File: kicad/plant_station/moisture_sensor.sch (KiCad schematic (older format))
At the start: 29 parts, among them IC3 TLC555CDR, IC4 ADC081C021CIMK_NOPB, IC5 IQS263B-0-DNR, IC6 CAP1293-1-AC3-TR

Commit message: Board v.2 sent for printing
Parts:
- removed J?: Conn_02x08_Counter_Clockwise, symbol Connector_Generic:Conn_02x08_Counter_Clockwise
- added J3: Conn_02x08_Odd_Even, Connector_PinHeader_2.54mm:PinHeader_2x08_P2.54mm_Vertical, symbol Connector_Generic:Conn_02x08_Odd_Even
- added J7: Samtec CES-104-01-T-D, Connector_PinSocket_2.54mm:PinSocket_2x04_P2.54mm_Vertical, symbol Connector_Generic:Conn_02x04_Odd_Even
- C4: value 1uF -> 1μF; footprint (none) -> Capacitor_SMD:C_1206_3216Metric
- C5, Cref1: footprint (none) -> Capacitor_SMD:C_1206_3216Metric
- C6: renamed from C?; value 1uF -> 1μF; footprint (none) -> Capacitor_SMD:C_1206_3216Metric
- C7: renamed from C?; value 0.1uF -> 0.1μF; footprint (none) -> Capacitor_SMD:C_1206_3216Metric
- Cdec1: value 0.1uF -> 0.1μF; footprint (none) -> Capacitor_SMD:C_1206_3216Metric
- Cdec2: renamed from Cdec?; value 4.7uF -> 4.7μF; footprint (none) -> Capacitor_SMD:C_1206_3216Metric
- IC6: footprint SON50P300X200X80-9N -> LocalsLib:CAP1293-1-AC3-TR
- J1: renamed from J?; value Conn_01x05 -> Conn_01x05_555; footprint (none) -> Connector_PinHeader_2.54mm:PinHeader_1x05_P2.54mm_Vertical
- J2: renamed from J?; value IQS263 -> Conn_01x04_IQS263; footprint (none) -> Connector_PinHeader_2.54mm:PinHeader_1x04_P2.54mm_Vertical
- J4: renamed from J?; value Conn_01x02 -> Conn_01x02_Sensor; footprint (none) -> Connector_PinHeader_2.54mm:PinHeader_1x02_P2.54mm_Vertical
- J5: renamed from J?; value CAP1293 -> Conn_01x03_CAP1293; footprint (none) -> Connector_PinHeader_2.54mm:PinHeader_1x03_P2.54mm_Vertical
- R10, R11, R5, R7, R8, R9: renamed from R?; footprint (none) -> Resistor_SMD:R_0805_2012Metric
- R12, R13: renamed from R?; value 10K? -> 4K7; footprint (none) -> Resistor_SMD:R_0805_2012Metric
- R4, Rb1: footprint (none) -> Resistor_SMD:R_1206_3216Metric
- R6: renamed from R?; value 5K? -> 4K7; footprint (none) -> Resistor_SMD:R_0805_2012Metric
- Ra1: footprint (none) -> Resistor_SMD:R_0805_2012Metric
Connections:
- net labels added: +3.3V, Sensor_Inside, Sensor_Outside
- wire segments 121 -> 118
- no-connect marks 0 -> 2
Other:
- note added: "Capacitor Inside\nPlate"
- note added: "Capacitor Outside\nPlate"
- note added: "Moisture Sensor"
- note removed: "Capacitor In Pin"
- note removed: "Capacitor Out Pin"
- moved on the sheet: C4, C5, C6, C7, Cdec1, Cdec2, Cref1, D1, IC3, IC4, J2, J4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

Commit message: Started working on v3 - added ADC081 driver and removed CAP and IQS chips
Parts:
- removed C6: 1μF, Capacitor_SMD:C_1206_3216Metric, symbol Device:C
- removed C7: 0.1μF, Capacitor_SMD:C_1206_3216Metric, symbol Device:C
- removed IC5: IQS263B-0-DNR, SamacSys:SON50P300X300X80-11N-D, symbol SamaSys:IQS263B-0-DNR
- removed IC6: CAP1293-1-AC3-TR, LocalsLib:CAP1293-1-AC3-TR, symbol LocalsLib:CAP1293-1-AC3-TR
- removed J2: Conn_01x04_IQS263, Connector_PinHeader_2.54mm:PinHeader_1x04_P2.54mm_Vertical, symbol Connector_Generic:Conn_01x04
- removed J3: Conn_02x08_Odd_Even, Connector_PinHeader_2.54mm:PinHeader_2x08_P2.54mm_Vertical, symbol Connector_Generic:Conn_02x08_Odd_Even
- removed J5: Conn_01x03_CAP1293, Connector_PinHeader_2.54mm:PinHeader_1x03_P2.54mm_Vertical, symbol Connector_Generic:Conn_01x03
- removed R10, R7, R8, R9: 470, Resistor_SMD:R_0805_2012Metric, symbol Device:R
- removed R11: 42.2, Resistor_SMD:R_0805_2012Metric, symbol Device:R
- removed R12, R13: 4K7, Resistor_SMD:R_0805_2012Metric, symbol Device:R
- Cdec2: footprint Capacitor_SMD:C_1206_3216Metric -> (none)
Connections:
- wire segments 118 -> 58
- no-connect marks 2 -> 0
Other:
- note added: "I2C ADDR 0x54"

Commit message: v3 schematics complete, USB breakout PCB designed
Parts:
- removed Cdec2: 4.7μF, symbol Device:C
- removed J1: Conn_01x05_555, Connector_PinHeader_2.54mm:PinHeader_1x05_P2.54mm_Vertical, symbol Connector_Generic:Conn_01x05
- removed J4: Conn_01x02_Sensor, Connector_PinHeader_2.54mm:PinHeader_1x02_P2.54mm_Vertical, symbol Connector_Generic:Conn_01x02
- removed J7: Samtec CES-104-01-T-D, Connector_PinSocket_2.54mm:PinSocket_2x04_P2.54mm_Vertical, symbol Connector_Generic:Conn_02x04_Odd_Even
- removed R6: 4K7, Resistor_SMD:R_0805_2012Metric, symbol Device:R
- added C7: 4.7uF, Capacitor_SMD:C_1206_3216Metric, symbol Device:C
- added D10: LS4148, Parts:MELF_SOD_80_3_BZT55B13GS08, symbol Device:D_Small
- added FB1, FB2: BLM21AG601SZ1D, Parts:Ferrite_Bead_0805_BLM21, symbol Device:Ferrite_Bead
- added J11: SOIL_I2C, Parts:Molex_Conn_SMD_01x06_505567_0671, symbol Parts:505567-0671
- added Q1: DTC113Z, Parts:DTC113ZEBTL, symbol Transistor_BJT:DTC113Z
- D1: footprint Diode_SMD:D_MELF -> Parts:MELF_SOD_80_3_BZT55B13GS08
- renumbered Cdec1 to C3
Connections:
- net labels added: ALL_EN, GNDA, HOST_WAKE, VA, VDD
- net labels removed: +3.3V, +3V3, 555_ALERT, CAP_ALERT, IQS_RDY
- wire segments 58 -> 40
- no-connect marks 0 -> 2
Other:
- note removed: "Capacitor Inside\nPlate"
- note removed: "Capacitor Outside\nPlate"
- moved on the sheet: C3, C4, C5, Cref1, D1, IC3, IC4, R4, R5, Ra1, Rb1

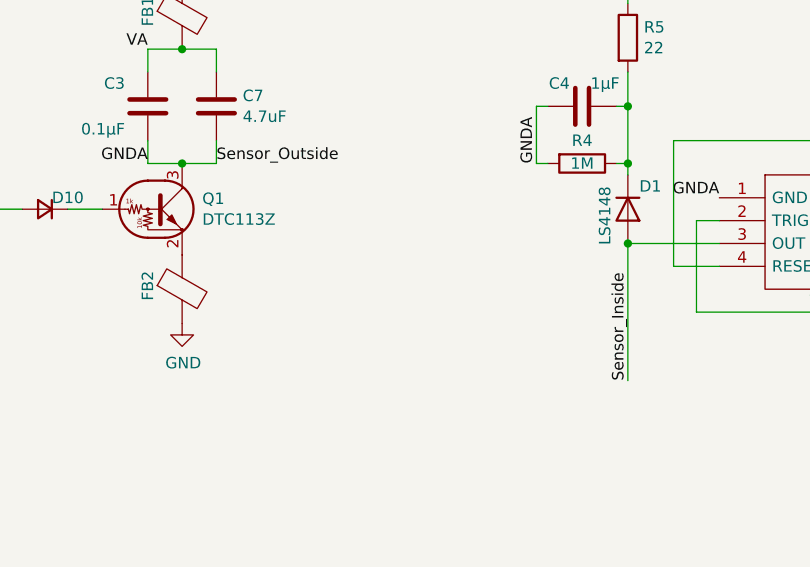
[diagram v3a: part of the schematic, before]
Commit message: Moved the LED driver to LEDs board, refactored connectors. Hopefuly PCBNEW could update it all in place
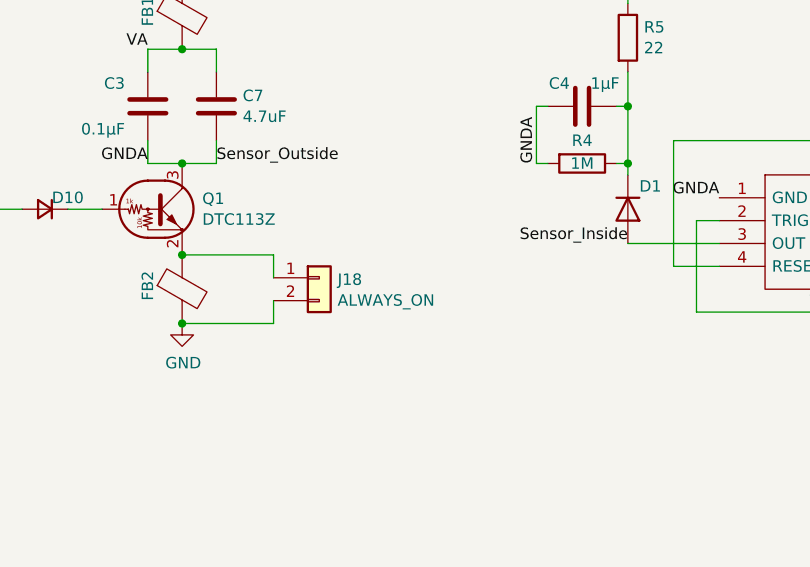
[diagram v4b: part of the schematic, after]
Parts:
- added J18: ALWAYS_ON, Connector_PinHeader_2.54mm:PinHeader_1x02_P2.54mm_Vertical, symbol Connector_Generic:Conn_01x02
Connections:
- net GND: now also J18.2 (Pin_2)
- net at FB2.1, Q1.2 (E): now also J18.1 (Pin_1)
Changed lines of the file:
@@
 P 7150 3900
 F 0 "D1" V 7050 3950 50  0000 L CNN
-F 1 "LS4148" H 7050 3800 50  0000 L CNN
+F 1 "LS4148" H 7050 3800 50  0001 L CNN
 F 2 "Parts:MELF_SOD_80_3_BZT55B13GS08" H 7150 3900 50  0001 C CNN
 F 3 "~" H 7150 3900 50  0001 C CNN
@@
 Wire Wire Line
 	5050 3200 5050 3300
-Text Label 7150 4650 1    50   ~ 0
+Text Label 7150 4050 2    50   ~ 0
 Sensor_Inside
 Text Label 5350 3700 0    50   ~ 0
@@
 Text Label 4400 3900 2    50   ~ 0
 ALL_EN
-Wire Wire Line
-	7150 4050 7150 4650
-Connection ~ 7150 4050
 Text Label 6750 3700 1    50   ~ 0
 GNDA
@@
 	1    0    0    -1
 $EndComp
+$Comp
+L Connector_Generic:Conn_01x02 J18
+U 1 1 5F4FBEBB
+P 5800 4200
+F 0 "J18" H 5880 4192 50  0000 L CNN
+F 1 "ALWAYS_ON" H 5880 4101 50  0000 L CNN
+F 2 "Connector_PinHeader_2.54mm:PinHeader_1x02_P2.54mm_Vertical" H 5800 4200 50  0001 C CNN
+F 3 "~" H 5800 4200 50  0001 C CNN
+	1    5800 4200
+	1    0    0    -1
+$EndComp
+Wire Wire Line
+	5200 4100 5600 4100
+Wire Wire Line
+	5600 4100 5600 4200
+Connection ~ 5200 4100
+Wire Wire Line
+	5600 4300 5600 4400
+Wire Wire Line
+	5600 4400 5200 4400
+Connection ~ 5200 4400
 $EndSCHEMATC

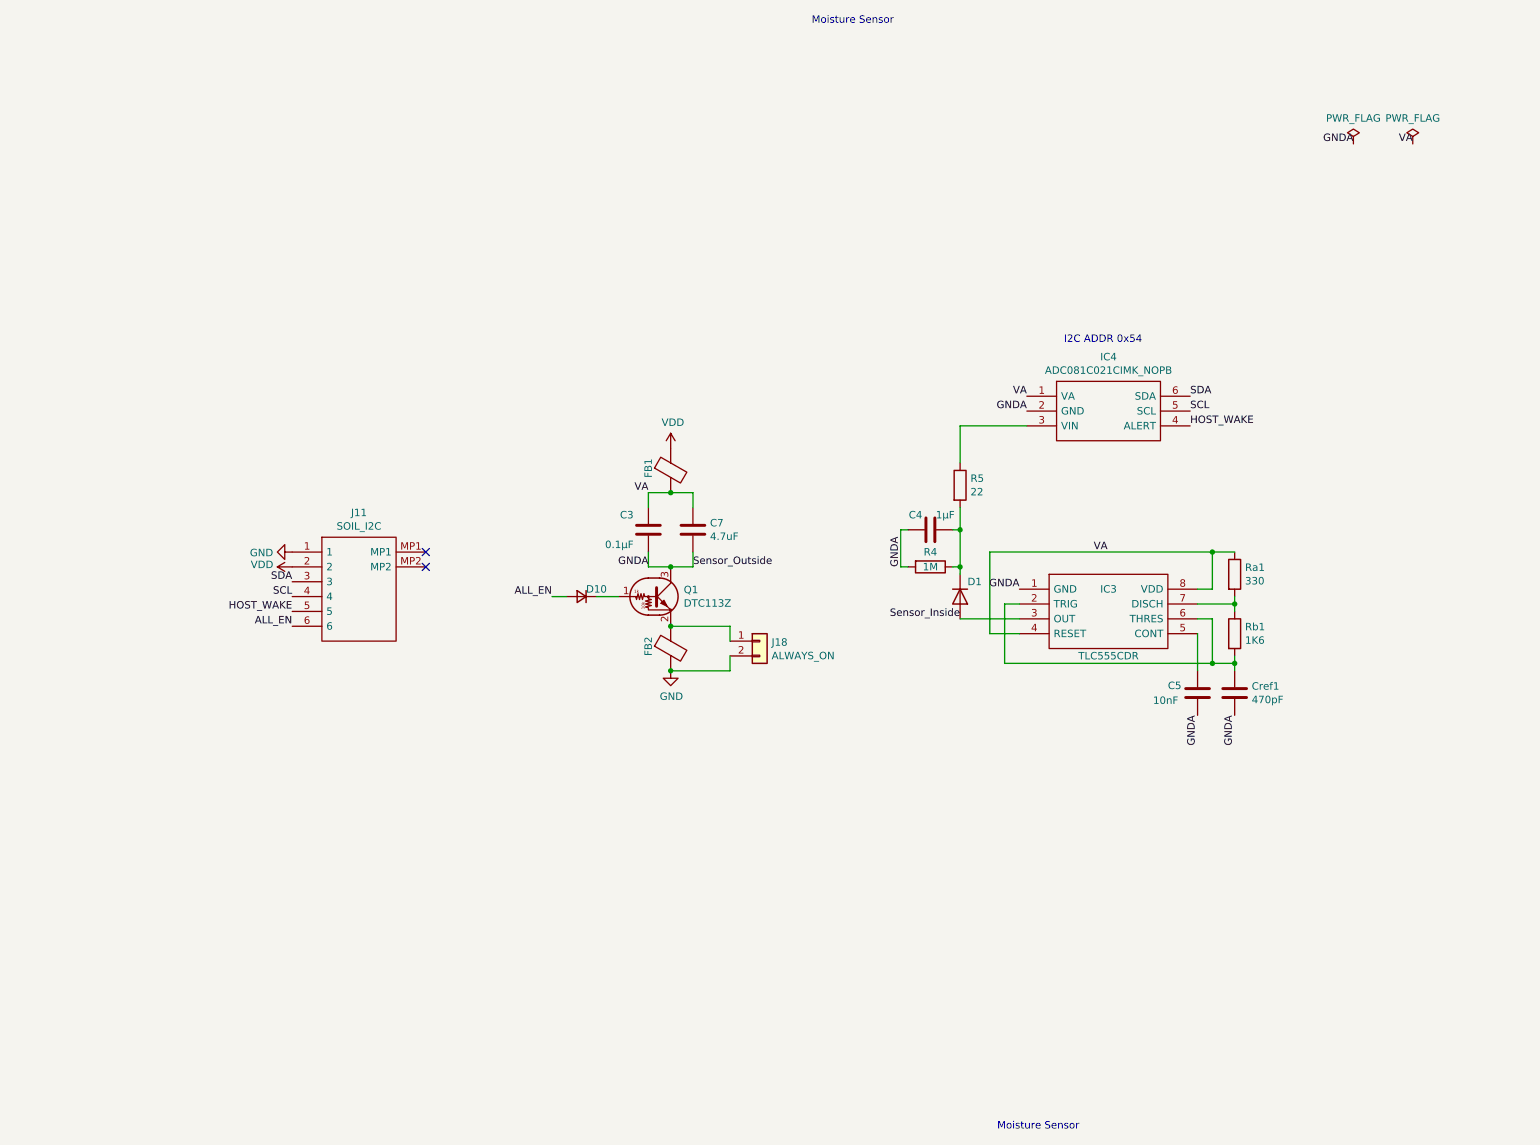
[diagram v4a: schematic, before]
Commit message: Pre-refactoring, diagnostics complete, timer not working properly
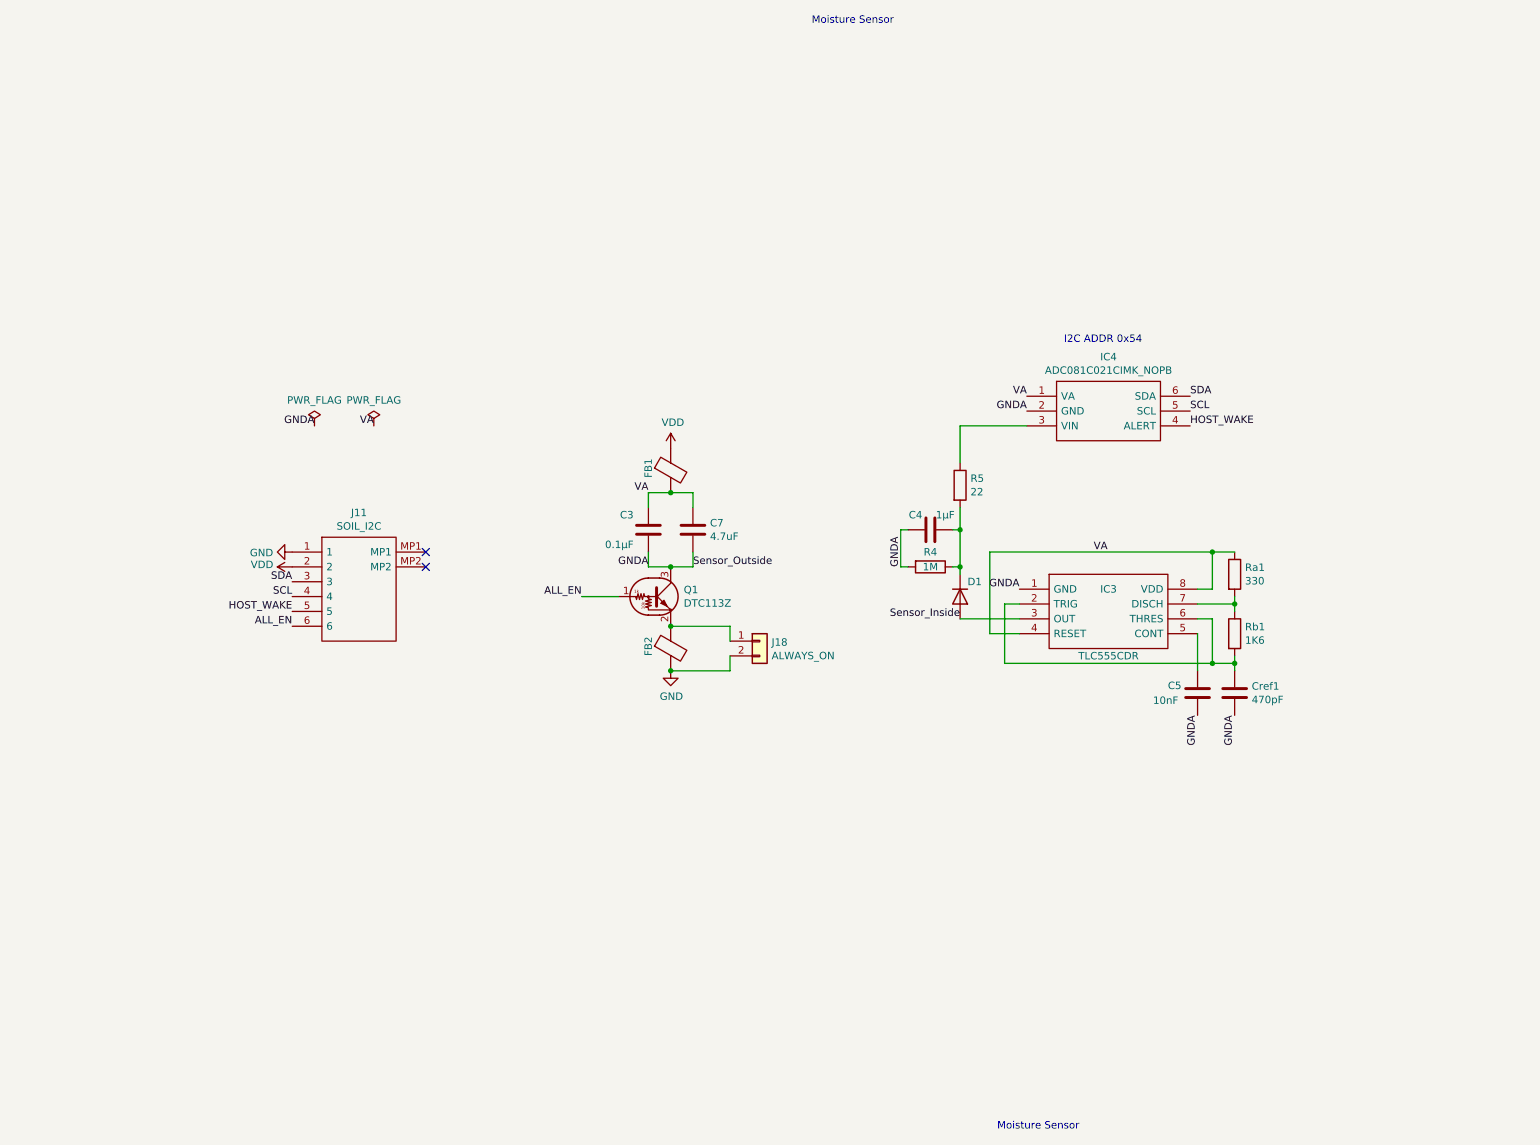
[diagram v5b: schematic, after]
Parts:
- removed D10: LS4148, Parts:MELF_SOD_80_3_BZT55B13GS08, symbol Device:D_Small
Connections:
- net ALL_EN: now also Q1.1 (B)
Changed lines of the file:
@@
 Wire Wire Line
 	5200 3700 5050 3700
-Wire Wire Line
-	4400 3900 4500 3900
 Text Label 5050 3700 2    50   ~ 0
 GNDA
@@
 Text Label 9000 4700 3    50   ~ 0
 GNDA
-Wire Wire Line
-	4700 3900 4850 3900
-$Comp
-L Device:D_Small D10
-U 1 1 6035AAFA
-P 4600 3900
-F 0 "D10" H 4500 3850 50  0000 C CNN
-F 1 "LS4148" H 4600 3784 50  0001 C CNN
-F 2 "Parts:MELF_SOD_80_3_BZT55B13GS08" V 4600 3900 50  0001 C CNN
-F 3 "~" V 4600 3900 50  0001 C CNN
-	1    4600 3900
-	-1   0    0    1
-$EndComp
 $Comp
 L power:GND #PWR?
@@
 Text Label 8700 2750 0    50   ~ 0
 HOST_WAKE
-Text Label 4400 3900 2    50   ~ 0
+Text Label 4600 3900 2    50   ~ 0
 ALL_EN
 Text Label 6750 3700 1    50   ~ 0
@@
 L power:PWR_FLAG #FLG0103
 U 1 1 606F4821
-P 9800 850
-F 0 "#FLG0103" H 9800 925 50  0001 C CNN
-F 1 "PWR_FLAG" H 9800 1023 50  0000 C CNN
-F 2 "" H 9800 850 50  0001 C CNN
-F 3 "~" H 9800 850 50  0001 C CNN
-	1    9800 850
+P 2800 2750
+F 0 "#FLG0103" H 2800 2825 50  0001 C CNN
+F 1 "PWR_FLAG" H 2800 2923 50  0000 C CNN
+F 2 "" H 2800 2750 50  0001 C CNN
+F 3 "~" H 2800 2750 50  0001 C CNN
+	1    2800 2750
 	1    0    0    -1
 $EndComp
@@
 L power:PWR_FLAG #FLG0104
 U 1 1 606F55AA
-P 10200 850
-F 0 "#FLG0104" H 10200 925 50  0001 C CNN
-F 1 "PWR_FLAG" H 10200 1023 50  0000 C CNN
-F 2 "" H 10200 850 50  0001 C CNN
-F 3 "~" H 10200 850 50  0001 C CNN
-	1    10200 850
+P 3200 2750
+F 0 "#FLG0104" H 3200 2825 50  0001 C CNN
+F 1 "PWR_FLAG" H 3200 2923 50  0000 C CNN
+F 2 "" H 3200 2750 50  0001 C CNN
+F 3 "~" H 3200 2750 50  0001 C CNN
+	1    3200 2750
 	1    0    0    -1
 $EndComp
-Text Label 9800 850  2    50   ~ 0
+Text Label 2800 2750 2    50   ~ 0
 GNDA
-Text Label 10200 850  2    50   ~ 0
+Text Label 3200 2750 2    50   ~ 0
 VA
 $Comp
@@
 	5600 4400 5200 4400
 Connection ~ 5200 4400
+Wire Wire Line
+	4600 3900 4850 3900
 $EndSCHEMATC
